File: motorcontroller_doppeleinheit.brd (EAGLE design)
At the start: 160 x 100 mm, 21 parts

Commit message: ...
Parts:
- removed QG1: 16,384Mhz, crystal:DIL14S
- added C3, C4: 22pF, rcl:C1206
- added Q1: 16,384Mhz, crystal:HC49UP
- added R3: 10k, rcl:R1206
- C1: device rcl:C075-032X103 -> rcl:C1206
- R1: device rcl:0207/12 -> rcl:C1206
- R2: device rcl:0207/12 -> rcl:R1206
- U$1: value TINY2313-*P* -> TINY2313-*S*; device avr-7:DIL20 -> avr-7:SO20L$
- moved C2 74.8 mm to (5.08, 33.0), turned to 270 degrees
- moved PHOTO1 72.1 mm to (71.1, 22.9), turned to 90 degrees
- moved R2 62.7 mm to (58.4, 2.54), flipped to the bottom, turned to 0 degrees
- moved LASER1 55.9 mm to (69.8, 16.5), turned to 0 degrees
- moved PHOTO2 55.0 mm to (71.1, 34.3), turned to 90 degrees
- moved CONTROLLER1 52.3 mm to (59.7, 22.9), turned to 90 degrees
- moved LASER2 52.2 mm to (69.8, 48.3), turned to 0 degrees
- moved ISP 51.8 mm to (44.5, 27.9), turned to 90 degrees
- moved LED1 50.6 mm to (64.8, 3.81), turned to 90 degrees
- moved U$2 42.2 mm to (21.6, 47.0), turned to 0 degrees
- moved U$1 41.0 mm to (24.1, 25.4), flipped to the bottom, turned to 180 degrees
- moved CONTROLLER2 40.4 mm to (59.7, 44.5), turned to 90 degrees
- moved AD9834 39.5 mm to (27.9, 6.35), turned to 0 degrees
- moved MOTOR_PCB 38.2 mm to (48.3, 52.1), turned to 270 degrees
- moved C1 38.1 mm to (10.2, 26.7), flipped to the bottom, turned to 270 degrees
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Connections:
- new net N$5: C3.2, Q1.2, U$1.4
- net +5V: now also R3.2; no longer QG1.14
- net GND: now also C3.1, C4.1; no longer QG1.7
- net LOCKED: now also R3.1
- net N$1: now also C4.2, Q1.1; no longer QG1.8
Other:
- board size 160 x 100 mm -> 75 x 65 mm

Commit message: ...
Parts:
- moved ISP 32.4 mm to (20.3, 6.35), turned to 0 degrees
- moved EXT-CLOCK 24.2 mm to (48.3, 29.2)
- moved AD9834 18.2 mm to (35.6, 22.9), turned to 90 degrees
- moved C1 16.2 mm to (21.6, 15.2), turned to 0 degrees
- moved RESET 8.13 mm to (5.08, 21.6)
- moved R1 2.84 mm to (12.7, 25.4), turned to 180 degrees
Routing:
- net +5V: track 0.00 -> 140.2 mm, vias 0 -> 2
- net OPTO1: track 0.00 -> 74.5 mm, vias 0 -> 3
- net +12V: track 0.00 -> 69.7 mm
- net OPTO2: track 0.00 -> 65.2 mm
- net LOCKED: track 0.00 -> 64.1 mm
- net +24V: track 0.00 -> 60.3 mm, vias 0 -> 1
- net RST: track 0.00 -> 53.1 mm
- net MOTOR_EN: track 0.00 -> 50.5 mm, vias 0 -> 1
- net SCK: track 0.00 -> 42.3 mm
- net SPEED_CLK: track 0.00 -> 41.3 mm
- net MOTOR_ON: track 0.00 -> 35.8 mm
- net N$3: track 0.00 -> 34.4 mm
- net LASER1+: track 0.00 -> 31.3 mm
- net MISO: track 0.00 -> 23.5 mm
- net LASER2+: track 0.00 -> 21.9 mm
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- added copper zone on layer 16, net GND

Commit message: ...
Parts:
- removed RESET: (no value), switch-omron:B3F-10XX
- ISP: device con-ml:ML6 -> con-harting-ml:ML6L
- R1: device rcl:C1206 -> rcl:R1206
- moved ISP 5.46 mm to (23.5, 10.8), turned to 180 degrees
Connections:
- net GND: no longer RESET.3, RESET.4
- net RST: no longer RESET.1, RESET.2
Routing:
- net RST: track 53.1 -> 34.7 mm, vias 0 -> 1
- net MISO: track 23.5 -> 12.3 mm
- net SCK: track 42.3 -> 38.2 mm, vias 0 -> 1
- net +5V: track 140.2 -> 142.0 mm
- net MOTOR_EN: track 50.5 -> 52.0 mm
- net OPTO1: track 74.5 -> 73.8 mm
- net MOSI: track 18.8 -> 18.1 mm

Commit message: ..
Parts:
- moved LED1 5.71 mm to (64.8, 9.53), turned to 180 degrees
- moved TP1 5.48 mm to (26.7, 55.5)
- moved C2 2.54 mm to (5.08, 30.5)
- moved U$2 2.54 mm to (21.6, 44.5)
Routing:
- net +12V: track 69.7 -> 56.7 mm
- net N$2: track 4.93 -> 12.4 mm
- net OPTO1: track 73.8 -> 70.8 mm
- net +24V: track 60.3 -> 62.4 mm
- net LOCKED: track 64.1 -> 62.1 mm
- net OPTO2: track 65.2 -> 64.2 mm
- net SPEED_CLK: track 41.0 -> 41.9 mm

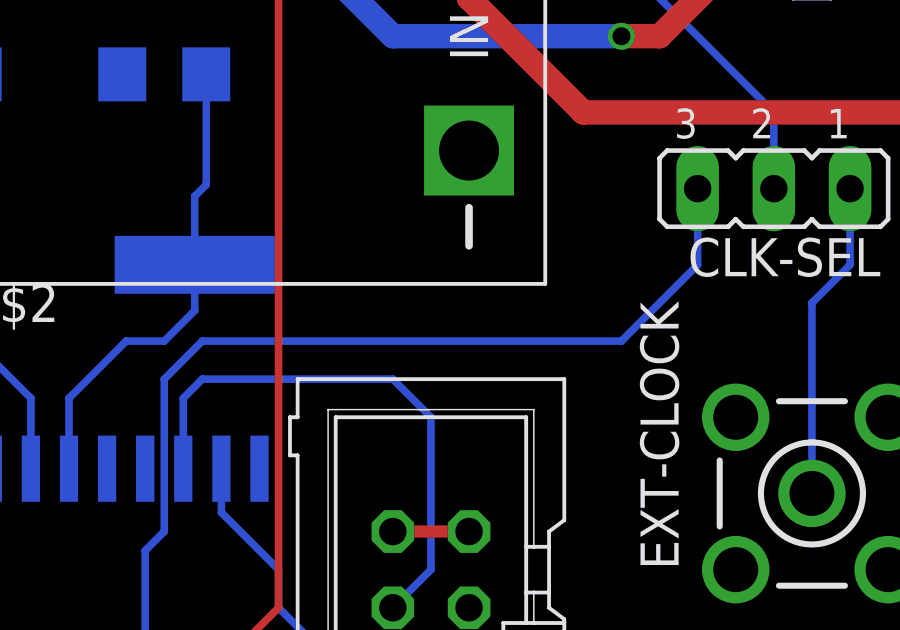
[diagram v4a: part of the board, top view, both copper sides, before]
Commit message: Added C5, modified firmware because of inverted logic
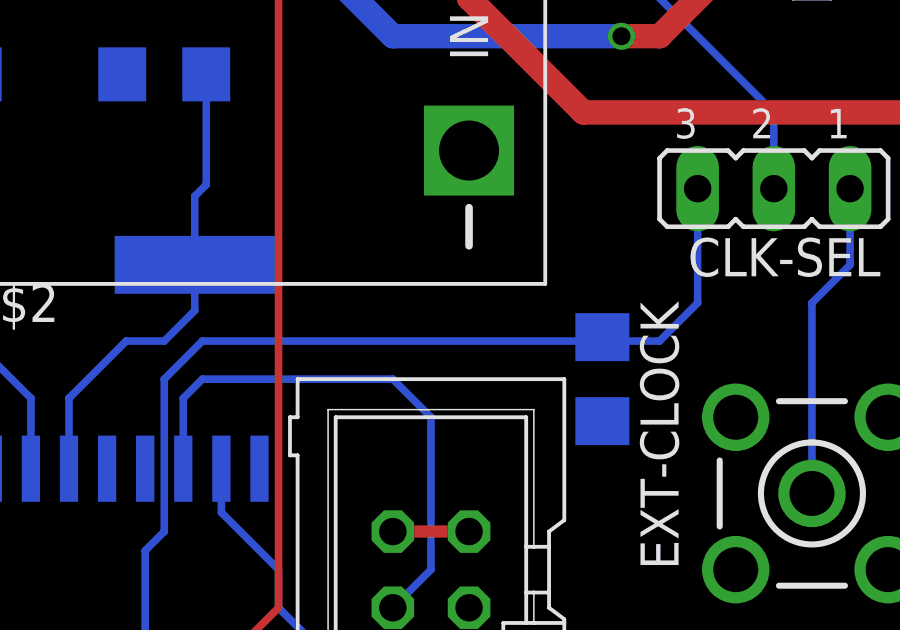
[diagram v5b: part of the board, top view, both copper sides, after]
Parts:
- added C5: 1n, rcl:C1206
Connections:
- net GND: now also C5.2
- net N$3: now also C5.1
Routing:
- net N$3: track 34.4 -> 35.3 mm
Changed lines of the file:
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@@
 <layer number="17" name="Pads" color="2" fill="1" visible="yes" active="yes"/>
 <layer number="18" name="Vias" color="2" fill="1" visible="yes" active="yes"/>
-<layer number="19" name="Unrouted" color="6" fill="1" visible="no" active="yes"/>
+<layer number="19" name="Unrouted" color="6" fill="1" visible="yes" active="yes"/>
 <layer number="20" name="Dimension" color="15" fill="1" visible="yes" active="yes"/>
-<layer number="21" name="tPlace" color="7" fill="1" visible="no" active="yes"/>
-<layer number="22" name="bPlace" color="7" fill="1" visible="no" active="yes"/>
-<layer number="23" name="tOrigins" color="15" fill="1" visible="no" active="yes"/>
-<layer number="24" name="bOrigins" color="15" fill="1" visible="no" active="yes"/>
-<layer number="25" name="tNames" color="7" fill="1" visible="no" active="yes"/>
-<layer number="26" name="bNames" color="7" fill="1" visible="no" active="yes"/>
-<layer number="27" name="tValues" color="7" fill="1" visible="no" active="yes"/>
-<layer number="28" name="bValues" color="7" fill="1" visible="no" active="yes"/>
-<layer number="29" name="tStop" color="7" fill="3" visible="no" active="yes"/>
-<layer number="30" name="bStop" color="7" fill="6" visible="no" active="yes"/>
-<layer number="31" name="tCream" color="7" fill="4" visible="no" active="yes"/>
-<layer number="32" name="bCream" color="7" fill="5" visible="no" active="yes"/>
-<layer number="33" name="tFinish" color="6" fill="3" visible="no" active="yes"/>
-<layer number="34" name="bFinish" color="6" fill="6" visible="no" active="yes"/>
-<layer number="35" name="tGlue" color="7" fill="4" visible="no" active="yes"/>
-<layer number="36" name="bGlue" color="7" fill="5" visible="no" active="yes"/>
-<layer number="37" name="tTest" color="7" fill="1" visible="no" active="yes"/>
-<layer number="38" name="bTest" color="7" fill="1" visible="no" active="yes"/>
-<layer number="39" name="tKeepout" color="4" fill="11" visible="no" active="yes"/>
-<layer number="40" name="bKeepout" color="1" fill="11" visible="no" active="yes"/>
-<layer number="41" name="tRestrict" color="4" fill="10" visible="no" active="yes"/>
-<layer number="42" name="bRestrict" color="1" fill="10" visible="no" active="yes"/>
-<layer number="43" name="vRestrict" color="2" fill="10" visible="no" active="yes"/>
-<layer number="44" name="Drills" color="7" fill="1" visible="no" active="yes"/>
-<layer number="45" name="Holes" color="7" fill="1" visible="no" active="yes"/>
-<layer number="46" name="Milling" color="3" fill="1" visible="no" active="yes"/>
-<layer number="47" name="Measures" color="7" fill="1" visible="no" active="yes"/>
-<layer number="48" name="Document" color="7" fill="1" visible="no" active="yes"/>
-<layer number="49" name="Reference" color="7" fill="1" visible="no" active="yes"/>
+<layer number="21" name="tPlace" color="7" fill="1" visible="yes" active="yes"/>
+<layer number="22" name="bPlace" color="7" fill="1" visible="yes" active="yes"/>
+<layer number="23" name="tOrigins" color="15" fill="1" visible="yes" active="yes"/>
+<layer number="24" name="bOrigins" color="15" fill="1" visible="yes" active="yes"/>
+<layer number="25" name="tNames" color="7" fill="1" visible="yes" active="yes"/>
+<layer number="26" name="bNames" color="7" fill="1" visible="yes" active="yes"/>
+<layer number="27" name="tValues" color="7" fill="1" visible="yes" active="yes"/>
+<layer number="28" name="bValues" color="7" fill="1" visible="yes" active="yes"/>
+<layer number="29" name="tStop" color="7" fill="3" visible="yes" active="yes"/>
+<layer number="30" name="bStop" color="7" fill="6" visible="yes" active="yes"/>
+<layer number="31" name="tCream" color="7" fill="4" visible="yes" active="yes"/>
+<layer number="32" name="bCream" color="7" fill="5" visible="yes" active="yes"/>
+<layer number="33" name="tFinish" color="6" fill="3" visible="yes" active="yes"/>
+<layer number="34" name="bFinish" color="6" fill="6" visible="yes" active="yes"/>
+<layer number="35" name="tGlue" color="7" fill="4" visible="yes" active="yes"/>
+<layer number="36" name="bGlue" color="7" fill="5" visible="yes" active="yes"/>
+<layer number="37" name="tTest" color="7" fill="1" visible="yes" active="yes"/>
+<layer number="38" name="bTest" color="7" fill="1" visible="yes" active="yes"/>
+<layer number="39" name="tKeepout" color="4" fill="11" visible="yes" active="yes"/>
+<layer number="40" name="bKeepout" color="1" fill="11" visible="yes" active="yes"/>
+<layer number="41" name="tRestrict" color="4" fill="10" visible="yes" active="yes"/>
+<layer number="42" name="bRestrict" color="1" fill="10" visible="yes" active="yes"/>
+<layer number="43" name="vRestrict" color="2" fill="10" visible="yes" active="yes"/>
+<layer number="44" name="Drills" color="7" fill="1" visible="yes" active="yes"/>
+<layer number="45" name="Holes" color="7" fill="1" visible="yes" active="yes"/>
+<layer number="46" name="Milling" color="3" fill="1" visible="yes" active="yes"/>
+<layer number="47" name="Measures" color="7" fill="1" visible="yes" active="yes"/>
+<layer number="48" name="Document" color="7" fill="1" visible="yes" active="yes"/>
+<layer number="49" name="Reference" color="7" fill="1" visible="yes" active="yes"/>
 <layer number="50" name="dxf" color="7" fill="1" visible="no" active="no"/>
-<layer number="51" name="tDocu" color="7" fill="1" visible="no" active="yes"/>
-<layer number="52" name="bDocu" color="7" fill="1" visible="no" active="yes"/>
+<layer number="51" name="tDocu" color="7" fill="1" visible="yes" active="yes"/>
+<layer number="52" name="bDocu" color="7" fill="1" visible="yes" active="yes"/>
 <layer number="90" name="Modules" color="5" fill="1" visible="no" active="no"/>
 <layer number="91" name="Nets" color="2" fill="1" visible="no" active="no"/>
@@
 <layer number="97" name="Info" color="7" fill="1" visible="no" active="no"/>
 <layer number="98" name="Guide" color="6" fill="1" visible="no" active="no"/>
-<layer number="101" name="Hidden" color="15" fill="1" visible="no" active="yes"/>
-<layer number="102" name="Changes" color="12" fill="1" visible="no" active="yes"/>
+<layer number="101" name="Hidden" color="15" fill="1" visible="yes" active="yes"/>
+<layer number="102" name="Changes" color="12" fill="1" visible="yes" active="yes"/>
 <layer number="200" name="200bmp" color="1" fill="10" visible="no" active="no"/>
 </layers>
@@
 <element name="C4" library="rcl" package="C1206" value="22pF" x="26.67" y="43.18" rot="MR180"/>
 <element name="R3" library="rcl" package="R1206" value="10k" x="58.42" y="7.62" rot="MR0"/>
+<element name="C5" library="rcl" package="C1206" value="1n" x="41.275" y="33.02" rot="MR270"/>
 </elements>
 <signals>
@@
 <wire x1="34.29" y1="27.94" x2="36.83" y2="27.94" width="0.4064" layer="1"/>
 <wire x1="58.42" y1="39.37" x2="60.96" y2="39.37" width="0.4064" layer="1"/>
+<contactref element="C5" pad="2"/>
 </signal>
 <signal name="N$1">
@@
 <wire x1="26.67" y1="27.94" x2="26.67" y2="33.02" width="0.254" layer="16"/>
 <wire x1="26.67" y1="33.02" x2="27.94" y2="34.29" width="0.254" layer="16"/>
-<wire x1="27.94" y1="34.29" x2="41.91" y2="34.29" width="0.254" layer="16"/>
-<wire x1="41.91" y1="34.29" x2="44.45" y2="36.83" width="0.254" layer="16"/>
-<wire x1="44.45" y1="36.83" x2="44.45" y2="39.37" width="0.254" layer="16"/>
+<wire x1="27.94" y1="34.29" x2="41.145" y2="34.29" width="0.254" layer="16"/>
+<contactref element="C5" pad="1"/>
+<wire x1="41.145" y1="34.29" x2="41.275" y2="34.42" width="0.254" layer="16"/>
+<wire x1="44.45" y1="39.37" x2="44.45" y2="35.56" width="0.254" layer="16"/>
+<wire x1="44.45" y1="35.56" x2="43.18" y2="34.29" width="0.254" layer="16"/>
+<wire x1="43.18" y1="34.29" x2="41.405" y2="34.29" width="0.254" layer="16"/>
+<wire x1="41.405" y1="34.29" x2="41.275" y2="34.42" width="0.254" layer="16"/>
 </signal>
 <signal name="N$4">
